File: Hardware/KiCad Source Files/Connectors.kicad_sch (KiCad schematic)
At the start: 8 parts, among them J1 YK3210203000G, J2 USB4085-GF-A, J3 Conn_01x08, J4 YK3210203000G, J5 USB4085-GF-A, J6 USB1125-GF-B

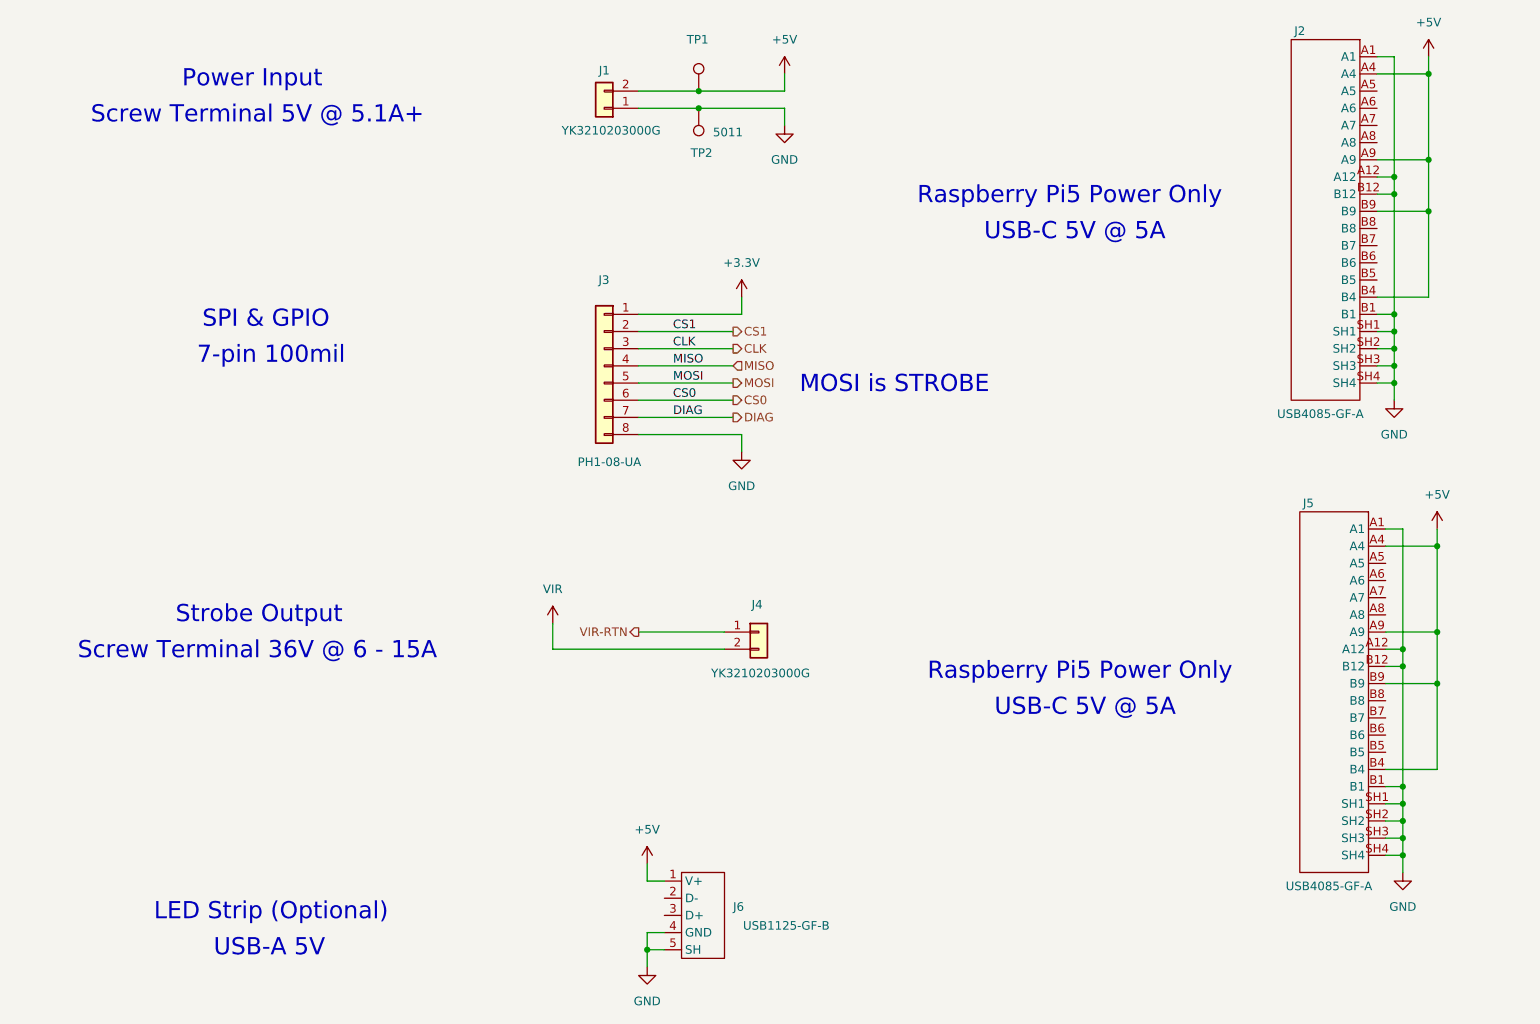
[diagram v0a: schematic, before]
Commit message: V3 connector board: strobe pulse limiter, USB-C fixes, boost protection
Mechanical: board outline, all mounting/tab/breakaway holes and every
existing part position are unchanged (checked against the previous revision);
all new parts are on the top side and no taller than existing parts.
PiTrac software compatibility: the LED current-control circuit and the
DAC/ADC/DIAG interface used by strobe_calibration_manager.py are unchanged.

Strobe (CC Sink sheet)
- AC-coupled pulse limiter: TRIG (DIAG/MOSI via D3/D4) -> C16 220nF ->
  GATE-DRV, R28 10K to GND (tau 2.2 ms). 8.7-130 us strobes and the
  calibration pulse pass (guaranteed >= ~0.38 ms by the MCP1407 input
  limits); a stuck-high DIAG turns the driver off after ~1.7 ms typical,
  <= ~2.8 ms worst case, so 10 A can no longer be held on.

USB-C (Connectors sheet, USB4085-GF-A footprint)
- J2/J5 feed 5 V to the Pis: add 10K Rp on CC1/CC2 (R24-R27, 1206).
- Footprint rebuilt to GCT's land pattern (16 plated 0.40/0.66 mm pins).
  The old VBUS/GND pads had 0.1 mm top-side copper (annular-ring DRC
  errors; Pi supply current only reached them via the barrel/bottom pad).

Boost (Power sheet)
- F1 MF-MSMF050-2 polyfuse in the boost input only (+5V_BST: C1/C2/C3/R1/
  U1); PCB: +5V_BST F.Cu island, +5V B.Cu bridge keeps the Pi feed width.
- D16 P4SMA39CA clamp on VIR (open-feedback fault; relies on F1).
- R5 2K49 -> 10K (was ~0.45 W in a 1/4 W resistor).

Housekeeping
- Project sym/fp-lib-tables; USB4085-GF-A added to the symbol library;
  pin types for custom parts; locally modified Q_NPN/Q_NMOS/LED moved into
  the project library (Q_NPN_EBC, Q_NMOS_SGD, LED_ThermalPad) to keep their
  numeric pinouts; no-connect flags; PWR_FLAGs; GATE-DRV wire to Q3 fixed.
- ERC pin map (project-wide): open emitter on a power rail allowed
  (MC33063 SwE to GND).
- Add V3 Connector Only.kicad_pro (board had no rules; DRC used defaults).
- Breakaway holes marked board-only.
- Regenerated Gerber/drill zips, BOM and centroid CSVs (same for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
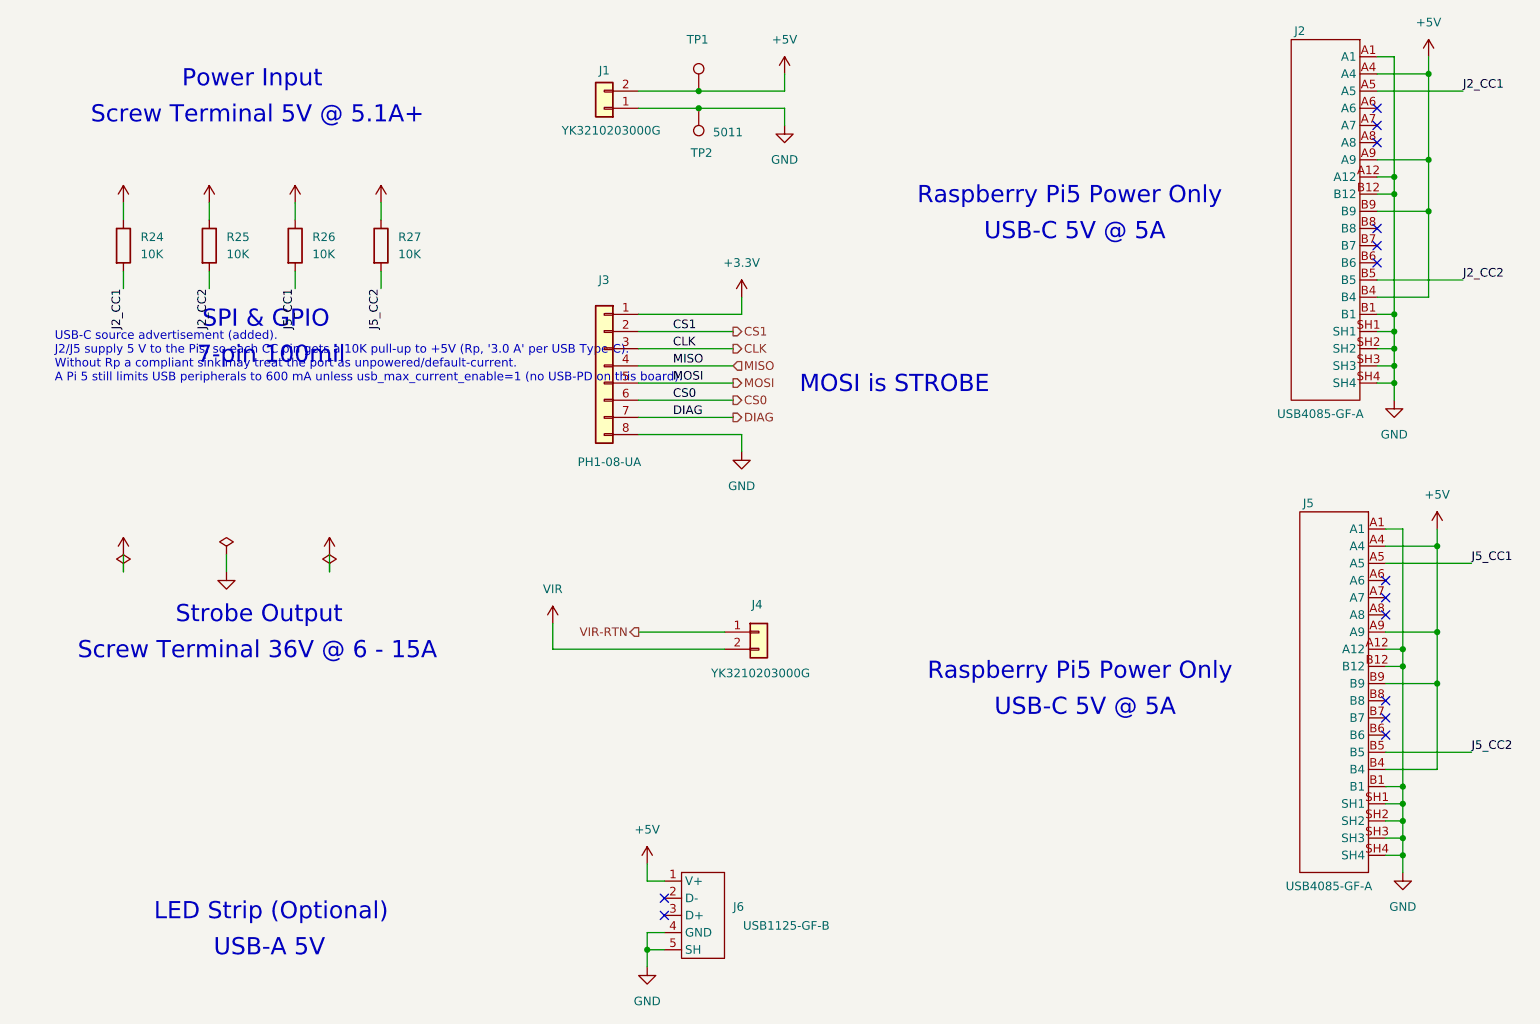
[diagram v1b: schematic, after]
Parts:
- added R24, R25, R26, R27: 10K, Resistor_SMD:R_1206_3216Metric_Pad1.30x1.75mm_HandSolder, symbol Device:R
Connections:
- net +5V: now also R24.1, R25.1, R26.1, R27.1
- net J5_CC1: now reaches J5.A5
- net J5_CC1: now also R26.2
- net J5_CC2: now reaches J5.B5
- net J5_CC2: now also R27.2
- net J2_CC1: now reaches J2.A5
- net J2_CC1: now also R24.2
- net J2_CC2: now reaches J2.B5
- net J2_CC2: now also R25.2
- no-connect marks 0 -> 14
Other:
- note added: "USB-C source advertisement (added). J2/J5 supply 5 V to the Pis, so each CC pin gets a 10K pull-up to +5V (Rp, '3.0 A' per USB Type-C). Without Rp a compliant sink may treat the port as unpowered/default-current. A Pi 5 still limits USB peripherals to 600 mA unless usb_max_current_enable=1 (no USB-PD on this board)."

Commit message: Address PR review: R5 part number, timing bounds, library defaults, ERC scope
- R5: PCB Part Number field still named the old MFR-25FTE52-2K49 on both
  boards; now MFR-25FRF52-10K, matching the schematic and BOM. (The stage-A
  update changed the value but not the BOM fields; no other part drifted.)
- Limiter note: worst-case bounds now include R28 1%, C16 +-10% plus X7R
  drift and a 2.7-2.95 V start level: cutoff <= ~3.2 ms, pass >= ~0.2 ms
  worst case (~1.7 ms typical for both).
- USB-C labels: "3A advertised (CC), 5A max" instead of "5A" — the Rp
  pull-ups advertise Type-C 3 A; the connector/copper are rated 5 A.
- Project library: default references Q4/Q1/D1 -> Q/Q/D; LED_ThermalPad
  default footprint -> Pi Connector Parts:VSMA1085400 (was an unresolvable
  Library:SST-10-IRD-B90H-S810). Sheet caches updated identically.
- ERC: revert the project-wide open-emitter/power-output relaxation and add a
  single exclusion for U1 pin 2 (MC33063 SwE to GND).
- V3 Connector Only.kicad_pro: own export folder and BOM file name.
- Regenerated Gerber zips and schematic PDF (BOM/centroid unchanged).

ERC 0 (1 intended exclusion). DRC both boards: 0 errors.

Co-Authored-By: Claude Opus 5.5 <noreply@anthropic.com>
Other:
- note added: "USB-C 5V: 3A advertised (CC), 5A max"
- note removed: "USB-C 5V @ 5A"
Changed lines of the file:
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@@
 		)
 	)
-	(text "USB-C 5V @ 5A"
+	(text "USB-C 5V: 3A advertised (CC), 5A max"
 		(exclude_from_sim no)
 		(at 181.356 58.928 0)
@@
 		)
 	)
-	(text "USB-C 5V @ 5A"
+	(text "USB-C 5V: 3A advertised (CC), 5A max"
 		(exclude_from_sim no)
 		(at 182.88 129.286 0)
